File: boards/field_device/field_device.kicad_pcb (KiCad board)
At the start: 4 copper layers, 40 parts, among them J1 Conn_01x05_Pin, U1 CHT20MEMS, U2 STM32C051F6P6, U3 SPA06-003, U4 CN3163, U5 HX8001-AJC

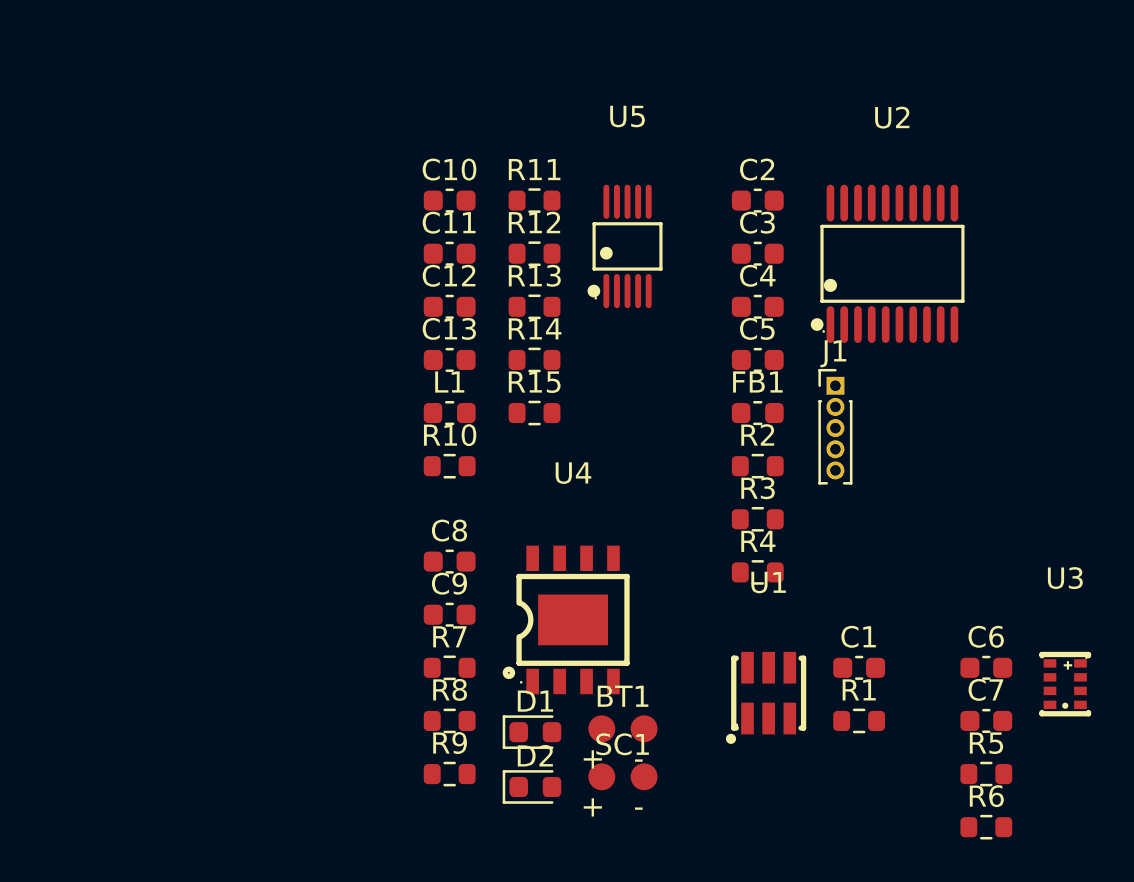
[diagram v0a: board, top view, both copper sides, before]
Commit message: removed 0 ohms resistors
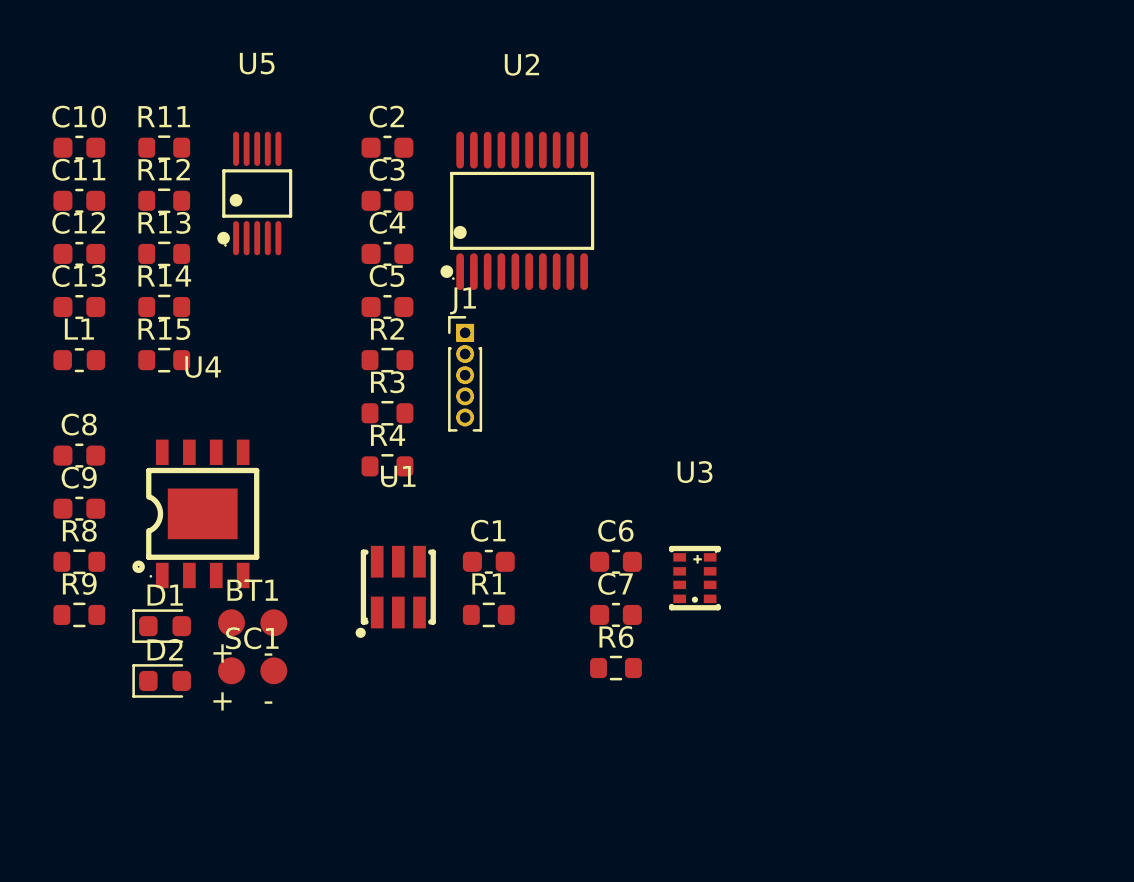
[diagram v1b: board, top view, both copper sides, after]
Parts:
- removed FB1: FerriteBead, Inductor_SMD:L_0603_1608Metric
- removed R10, R5, R7: 0Ω, Resistor_SMD:R_0603_1608Metric
- moved R9 19.0 mm to (132.5, 102.8)
- moved R6 19.0 mm to (157.9, 105.3)
- moved R8 19.0 mm to (132.5, 100.3)
- moved BT1 18.2 mm to (140.7, 103.2)
- moved C7 18.2 mm to (157.9, 102.8)
- moved C9 18.2 mm to (132.5, 97.8)
- moved D1 18.2 mm to (136.6, 103.4)
- moved D2 18.2 mm to (136.6, 106.0)
- moved R1 18.2 mm to (151.9, 102.8)
- moved R2 18.2 mm to (147.1, 90.8)
- moved R4 18.2 mm to (147.1, 95.8)
- moved SC1 18.2 mm to (140.7, 105.5)
- moved U1 18.2 mm to (147.6, 101.5)
- moved U3 18.2 mm to (161.6, 101.1)
- moved C1 18.2 mm to (151.9, 100.3)
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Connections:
- net /humidity_sensor/clean_pwr renamed Net-(U1-VDD)
- BT1 pad 1: /power_source/regulator/Vin -> /power_source/regulator/pwr
- C2 pad 1: /MCU/clean_pwr -> +3.3V
- C3 pad 1: /MCU/clean_pwr -> +3.3V
- C4 pad 1: /MCU/clean_pwr -> +3.3V
- C6 pad 1: /pressure_sensor/clean_pwr -> +3.3V
- C7 pad 1: /pressure_sensor/clean_pwr -> +3.3V
- C9 pad 1: /power_source/regulator/Vin -> /power_source/regulator/pwr
- R2 pad 1: /MCU/clean_pwr -> +3.3V
- SC1 pad 1: Net-(SC1-+) -> /power_source/solar_pwr
- U2 pad 4: /MCU/clean_pwr -> +3.3V
- U3 pad 6: /pressure_sensor/clean_pwr -> +3.3V
- U3 pad 8: /pressure_sensor/clean_pwr -> +3.3V
- U4 pad 5: /power_source/regulator/Vin -> /power_source/regulator/pwr
- U4 pad 8: /power_source/regulator/Vin -> /power_source/regulator/pwr

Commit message: fun
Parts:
- added AE1: Antenna, Package_DFN_QFN:DFN-8-1EP_2x3mm_P0.5mm_EP0.61x2.2mm, F.Cu at (184.5, 86.7)
- added C14: 1.5nF, Capacitor_SMD:C_0201_0603Metric, F.Cu at (196.1, 89.2)
- added C15: 22uF, Capacitor_SMD:C_0201_0603Metric, F.Cu at (196.1, 91.7)
- added C16: 470nF, Capacitor_SMD:C_0603_1608Metric, F.Cu at (172.4, 75.7)
- added C17: 10uF, Capacitor_SMD:C_0603_1608Metric, F.Cu at (172.4, 78.2)
- added C18: 100nF, Capacitor_SMD:C_0603_1608Metric, F.Cu at (172.4, 80.7)
- added C19: 100nF, Capacitor_SMD:C_0603_1608Metric, F.Cu at (172.4, 83.2)
- added C20: 100nF, Capacitor_SMD:C_0603_1608Metric, F.Cu at (176.4, 75.7)
- added C21: 47nF, Capacitor_SMD:C_0603_1608Metric, F.Cu at (176.4, 78.2)
- added C22: 100pF, Capacitor_SMD:C_0603_1608Metric, F.Cu at (176.4, 80.7)
- added C23: 100pF, Capacitor_SMD:C_0603_1608Metric, F.Cu at (176.4, 83.2)
- added C24: C_Shunt_1, Capacitor_SMD:C_0603_1608Metric, F.Cu at (180.4, 75.7)
- added C25: C_Shunt_2, Capacitor_SMD:C_0603_1608Metric, F.Cu at (180.4, 78.2)
- added L2: 47nH, Inductor_SMD:L_0603_1608Metric, F.Cu at (180.4, 80.7)
- added L3: L_Series, Inductor_SMD:L_0603_1608Metric, F.Cu at (180.4, 83.2)
- added R10: 1kΩ, Resistor_SMD:R_0603_1608Metric, F.Cu at (150.1, 99.5)
- added R16: 200kΩ, Resistor_SMD:R_0201_0603Metric, F.Cu at (200.1, 94.2)
- added R5: 10kΩ, Resistor_SMD:R_0603_1608Metric, F.Cu at (154.1, 85.7)
- added R7: 22Ω, Resistor_SMD:R_0603_1608Metric, F.Cu at (158.1, 78.2)
- added SW1: SW_SPST, UnEasy-LCSC:KEY-SMD_L3.9-W3.0-LS5.0-EH, F.Cu at (151.3, 89.1)
- added U6: SX1262IMLTRT, Package_DFN_QFN:QFN-24-1EP_4x4mm_P0.5mm_EP2.15x2.15mm, F.Cu at (173.9, 87.6)
- added Y1: Crystal_GND24, Crystal:Crystal_SMD_3225-4Pin_3.2x2.5mm, F.Cu at (179.7, 86.7)
- C10: value 10uF -> 1uF
- C11: value 100nF -> 1uF
- C12: value 1.5nF -> 10uF; footprint Capacitor_SMD:C_0603_1608Metric -> Capacitor_SMD:C_0201_0603Metric
- C13: value 22uF -> 100nF; footprint Capacitor_SMD:C_0603_1608Metric -> Capacitor_SMD:C_0201_0603Metric
- C8, C9: value 1uF -> 100nF
- L1: footprint Inductor_SMD:L_0603_1608Metric -> Inductor_SMD:L_0201_0603Metric
- R11: value 1MΩ -> 2kΩ
- R12: value 60.4kΩ -> 1MΩ; footprint Resistor_SMD:R_0603_1608Metric -> Resistor_SMD:R_0201_0603Metric
- R13: value 340kΩ -> 60.4kΩ; footprint Resistor_SMD:R_0603_1608Metric -> Resistor_SMD:R_0201_0603Metric
- R14: value 15kΩ -> 340kΩ; footprint Resistor_SMD:R_0603_1608Metric -> Resistor_SMD:R_0201_0603Metric
- R15: value 200kΩ -> 15kΩ; footprint Resistor_SMD:R_0603_1608Metric -> Resistor_SMD:R_0201_0603Metric
- R3, R4: value 0Ω -> 10kΩ
- R6: value 10kΩ? -> 22Ω
- R8: value 1kΩ -> 22Ω
- R9: value 2kΩ -> 10kΩ?
- moved C12 72.3 mm to (204.7, 81.8), turned to 180 degrees
- moved R12 68.2 mm to (204.7, 82.6), turned to 180 degrees
- moved L1 63.7 mm to (196.1, 94.2)
- moved U5 63.7 mm to (204.5, 86.4)
- moved C13 63.6 mm to (196.1, 86.7)
- moved R13 63.6 mm to (200.1, 86.7)
- moved R14 63.6 mm to (200.1, 89.2)
- moved R15 63.6 mm to (200.1, 91.7)
- moved C8 46.9 mm to (179.0, 101.8)
- moved C9 46.9 mm to (179.0, 104.3)
- moved R9 46.7 mm to (179.0, 106.9)
- moved C1 32.4 mm to (183.8, 94.5)
- moved R1 32.4 mm to (183.8, 97.0)
- moved U1 32.4 mm to (179.5, 95.7)
- moved R8 32.3 mm to (158.1, 80.7)
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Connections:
- C10 pad 1: /power_source/regulator/pwr -> /power_source/solar_pwr
- C11 pad 1: /power_source/regulator/enable -> /power_source/regulator/pwr
- C12 pad 1: Net-(U5-VC) -> /power_source/regulator/pwr
- C12 pad 2: Net-(C12-Pad2) -> GND
- C13 pad 1: +3.3V -> /power_source/regulator/enable
- C8 pad 1: /power_source/solar_pwr -> +3.3V
- C9 pad 1: /power_source/regulator/pwr -> +3.3V
- R11 pad 1: /power_source/regulator/pwr -> Net-(U4-ISET)
- R11 pad 2: /power_source/regulator/enable -> GND
- R12 pad 1: Net-(U5-RT) -> /power_source/regulator/pwr
- R12 pad 2: GND -> /power_source/regulator/enable
- R13 pad 1: Net-(U5-FB) -> Net-(U5-RT)
- R13 pad 2: +3.3V -> GND
- R14 pad 1: Net-(C12-Pad2) -> Net-(U5-FB)
- R14 pad 2: Net-(U5-FB) -> +3.3V
- R15 pad 1: Net-(U5-FB) -> Net-(C14-Pad2)
- R15 pad 2: GND -> Net-(U5-FB)
- R3 pad 1: /MCU/humidity_SDA -> /MCU/SDA_bus
- R3 pad 2: /MCU/SDA_bus -> +3.3V
- R4 pad 1: /MCU/humidity_SCL -> /MCU/SCL_bus
- R4 pad 2: /MCU/SCL_bus -> +3.3V
- R6 pad 1: +3.3V -> Net-(U2-PA7)
- R6 pad 2: Net-(U3-CSB) -> /MCU/RF_MOSI
- R8 pad 1: /power_source/solar_pwr -> Net-(U2-PA5)
- R8 pad 2: Net-(D1-A) -> /MCU/RF_SCK
- R9 pad 1: Net-(U4-ISET) -> +3.3V
- R9 pad 2: GND -> Net-(U3-CSB)
- U1 pad 3: /MCU/humidity_SCL -> /MCU/SCL_bus
- U1 pad 4: /MCU/humidity_SDA -> /MCU/SDA_bus
- U2 pad 10: unconnected-(U2-PA3-Pad10) -> /MCU/RF_BUSY
- U2 pad 11: unconnected-(U2-PA4-Pad11) -> /MCU/RF_NSS
- U2 pad 12: unconnected-(U2-PA5-Pad12) -> Net-(U2-PA5)
- U2 pad 13: unconnected-(U2-PA6-Pad13) -> Net-(U2-PA6)
- U2 pad 14: unconnected-(U2-PA7-Pad14) -> Net-(U2-PA7)
- U2 pad 8: unconnected-(U2-PA1-Pad8) -> /MCU/RF_DIO1
- U2 pad 9: unconnected-(U2-PA2-Pad9) -> /MCU/RF_NRST
- U3 pad 3: /MCU/humidity_SDA -> /MCU/SDA_bus
- U3 pad 4: /MCU/humidity_SCL -> /MCU/SCL_bus
- U5 pad 2: unconnected-(U5-MS-Pad2) -> GND

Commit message: forgo the power planes
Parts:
- moved R12 0.10 mm to (204.8, 82.7)
- moved C12 0.07 mm to (204.8, 81.8)
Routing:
- net /power_source/regulator/pwr: track 0.00 -> 2.39 mm
- net /power_source/regulator/enable: track 0.00 -> 1.71 mm
- net (no net): vias 0 -> 1
- added copper zone on In2.Cu, net +3.3V
- added copper zone on In1.Cu, net GND
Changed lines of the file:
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@@
 	(footprint "Resistor_SMD:R_0201_0603Metric"
 		(layer "F.Cu")
-		(at 204.74006 82.610373 180)
+		(at 204.787849 82.697014 180)
 		(descr "Resistor SMD 0201 (0603 Metric), square (rectangular) end terminal, IPC-7351 nominal, (Body size source: https://www.vishay.com/docs/20052/crcw0201e3.pdf)")
 		(tags "resistor")
@@
 	(footprint "Capacitor_SMD:C_0201_0603Metric"
 		(layer "F.Cu")
-		(at 204.736248 81.751255 180)
+		(at 204.785554 81.803054 180)
 		(descr "Capacitor SMD 0201 (0603 Metric), square (rectangular) end terminal, IPC-7351 nominal, (Body size source: https://www.vishay.com/docs/20052/crcw0201e3.pdf)")
 		(tags "capacitor")
 		(property "Reference" "C12"
-			(at 0 -1.05 0)
+			(at -2.210672 0.404351 0)
 			(layer "F.SilkS")
 			(effects
@@
 		(descr "C521274, HEXIN(禾芯微), HX8001-AJC, generated with UnEasy-LCSC")
 		(property "Reference" "U5"
-			(at 0 -6.11 0)
+			(at 2.54 0 0)
 			(layer "F.SilkS")
 			(effects
@@
 			)
 		)
+	)
+	(via blind
+		(at 203.667585 81.812532)
+		(size 0.6)
+		(drill 0.3)
+		(layers "F.Cu" "In1.Cu")
+		(net "")
+	)
+	(segment
+		(start 205.105554 81.803054)
+		(end 205.105554 82.694719)
+		(width 0.3)
+		(layer "F.Cu")
+		(net "/power_source/regulator/pwr")
+	)
+	(segment
+		(start 205.132849 82.818361)
+		(end 204.97 82.98121)
+		(width 0.3)
+		(layer "F.Cu")
+		(net "/power_source/regulator/pwr")
+	)
+	(segment
+		(start 205.105554 82.694719)
+		(end 205.107849 82.697014)
+		(width 0.2)
+		(layer "F.Cu")
+		(net "/power_source/regulator/pwr")
+	)
+	(segment
+		(start 204.97 82.98121)
+		(end 204.97 84.25)
+		(width 0.3)
+		(layer "F.Cu")
+		(net "/power_source/regulator/pwr")
+	)
+	(segment
+		(start 204.42006 84.20006)
+		(end 204.47 84.25)
+		(width 0.2)
+		(layer "F.Cu")
+		(net "/power_source/regulator/enable")
+	)
+	(segment
+		(start 204.47 82.641211)
+		(end 204.492849 82.618362)
+		(width 0.2)
+		(layer "F.Cu")
+		(net "/power_source/regulator/enable")
+	)
+	(segment
+		(start 204.47 84.25)
+		(end 204.47 82.641211)
+		(width 0.3)
+		(layer "F.Cu")
+		(net "/power_source/regulator/enable")
+	)
+	(zone
+		(net "GND")
+		(layer "In1.Cu")
+		(name "gnd")
+		(hatch edge 0.5)
+		(connect_pads
+			(clearance 0.5)
+		)
+		(min_thickness 0.25)
+		(fill
+			(thermal_gap 0.5)
+			(thermal_bridge_width 0.5)
+			(island_removal_mode 0)
+		)
+		(polygon
+			(pts
+				(xy 127 50.8) (xy 127 127) (xy 242.57 127) (xy 241.3 50.8)
+			)
+		)
+	)
+	(zone
+		(net "+3.3V")
+		(layer "In2.Cu")
+		(name "pwr")
+		(hatch edge 0.5)
+		(priority 1)
+		(connect_pads
+			(clearance 0.5)
+		)
+		(min_thickness 0.25)
+		(fill
+			(thermal_gap 0.5)
+			(thermal_bridge_width 0.5)
+			(island_removal_mode 0)
+		)
+		(polygon
+			(pts
+				(xy 127 50.8) (xy 127 127) (xy 242.57 127) (xy 241.3 50.8)
+			)
+		)
